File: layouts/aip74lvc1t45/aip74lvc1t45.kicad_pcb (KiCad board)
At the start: 2 copper layers, 3 parts

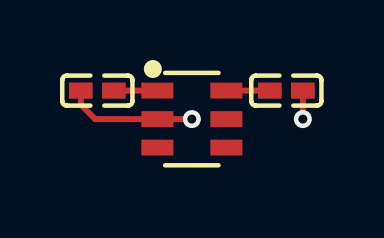
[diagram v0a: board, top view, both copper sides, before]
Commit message: fix: Update deps, swapped pinout (#2)
* rebuild with upstream rp2040 fixes. move header .25mm to the right. center dap-LED

* fix workflow triggers

* fix swapped jlink connector pinout + update deps

* pin atopile workflow version to v1.x.x
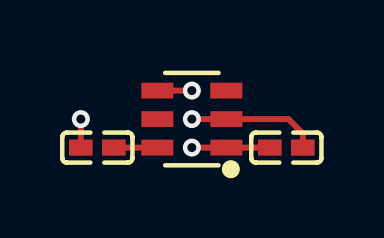
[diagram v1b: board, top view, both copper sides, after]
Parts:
- moved C2 6.58 mm to (-3.15, 0.95), turned to 180 degrees
- moved C1 6.58 mm to (3.15, 0.95), turned to 0 degrees
- turned U1 to 90 degrees
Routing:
- net B: track 0.00 -> 1.15 mm, vias 0 -> 1
- net power_a-VCC: track 1.45 -> 2.60 mm, vias 0 -> 1
